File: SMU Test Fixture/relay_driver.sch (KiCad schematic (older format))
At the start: 48 parts, among them U7 ADG1414BRU, U8 ADG1414BRU

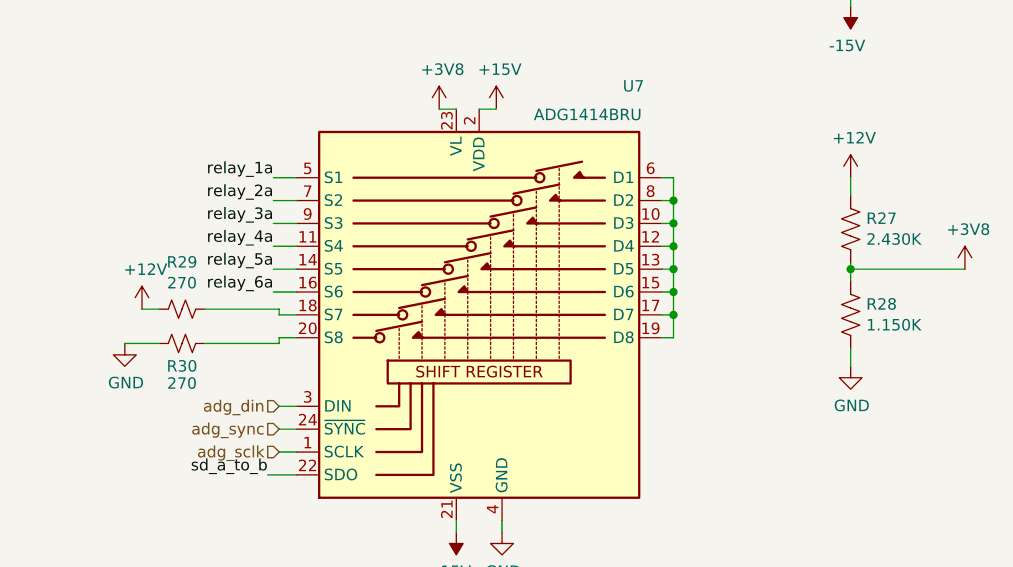
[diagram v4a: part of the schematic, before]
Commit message: Reannotate, power supply schematic improvements, begin power supply layout.
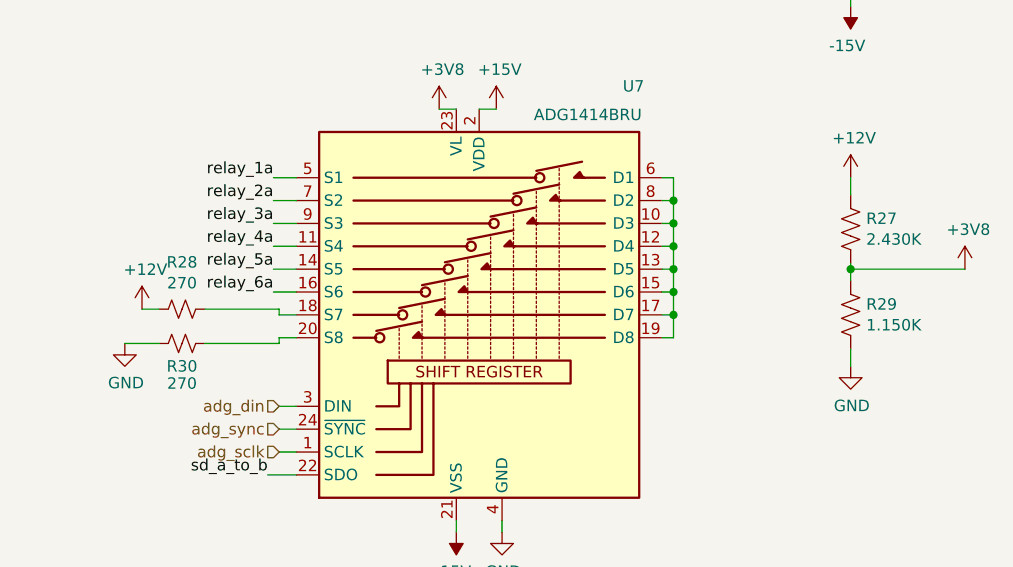
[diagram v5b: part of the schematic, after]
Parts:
- R27: footprint (none) -> Resistor_SMD:R_0805_2012Metric_Pad1.20x1.40mm_HandSolder
- R29: renamed from R28; footprint (none) -> Resistor_SMD:R_0805_2012Metric_Pad1.20x1.40mm_HandSolder
- renumbered R29 to R28
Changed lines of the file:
@@
 P 10425 700
 AR Path="/6011CEB7/6031CE6D" Ref="#PWR?"  Part="1"
-AR Path="/602F30C4/6031CE6D" Ref="#PWR046"  Part="1"
-F 0 "#PWR046" H 10425 550 50  0001 C CNN
+AR Path="/602F30C4/6031CE6D" Ref="#PWR045"  Part="1"
+F 0 "#PWR045" H 10425 550 50  0001 C CNN
 F 1 "+15V" H 10440 873 50  0000 C CNN
 F 2 "" H 10425 700 50  0001 C CNN
@@
 P 10425 1625
 AR Path="/6011CEB7/6031CE73" Ref="#PWR?"  Part="1"
-AR Path="/602F30C4/6031CE73" Ref="#PWR050"  Part="1"
-F 0 "#PWR050" H 10425 1725 50  0001 C CNN
+AR Path="/602F30C4/6031CE73" Ref="#PWR047"  Part="1"
+F 0 "#PWR047" H 10425 1725 50  0001 C CNN
 F 1 "-15V" H 10440 1798 50  0000 C CNN
 F 2 "" H 10425 1625 50  0001 C CNN
@@
 P 10200 1175
 AR Path="/6011CEB7/6031CE85" Ref="#PWR?"  Part="1"
-AR Path="/602F30C4/6031CE85" Ref="#PWR048"  Part="1"
-F 0 "#PWR048" H 10200 925 50  0001 C CNN
+AR Path="/602F30C4/6031CE85" Ref="#PWR046"  Part="1"
+F 0 "#PWR046" H 10200 925 50  0001 C CNN
 F 1 "GND" H 10205 1002 50  0000 C CNN
 F 2 "" H 10200 1175 50  0001 C CNN
@@
 	8000 2975 7925 2975
 $Comp
-L Device:R_Small_US R29
+L Device:R_Small_US R28
 U 1 1 63E80504
 P 7500 2950
-F 0 "R29" V 7295 2950 50  0000 C CNN
+F 0 "R28" V 7295 2950 50  0000 C CNN
 F 1 "270" V 7386 2950 50  0000 C CNN
 F 2 "Resistor_SMD:R_0805_2012Metric_Pad1.20x1.40mm_HandSolder" H 7500 2950 50  0001 C CNN
@@
 P 8875 2075
 AR Path="/6011CEB7/640AE01E" Ref="#PWR?"  Part="1"
-AR Path="/602F30C4/640AE01E" Ref="#PWR052"  Part="1"
-F 0 "#PWR052" H 8875 1925 50  0001 C CNN
+AR Path="/602F30C4/640AE01E" Ref="#PWR049"  Part="1"
+F 0 "#PWR049" H 8875 1925 50  0001 C CNN
 F 1 "+15V" H 8890 2248 50  0000 C CNN
 F 2 "" H 8875 2075 50  0001 C CNN
@@
 ext_meas_sel_b_r
 $Comp
-L power:GND #PWR054
+L power:GND #PWR053
 U 1 1 5FFD6724
 P 7250 3100
-F 0 "#PWR054" H 7250 2850 50  0001 C CNN
+F 0 "#PWR053" H 7250 2850 50  0001 C CNN
 F 1 "GND" H 7255 2927 50  0000 C CNN
 F 2 "" H 7250 3100 50  0001 C CNN
@@
 $EndComp
 $Comp
-L power:+12V #PWR053
+L power:+12V #PWR052
 U 1 1 60DAA752
 P 7325 2950
-F 0 "#PWR053" H 7325 2800 50  0001 C CNN
+F 0 "#PWR052" H 7325 2800 50  0001 C CNN
 F 1 "+12V" H 7340 3123 50  0000 C CNN
 F 2 "" H 7325 2950 50  0001 C CNN
@@
 F 0 "R27" H 10493 2646 50  0000 L CNN
 F 1 "2.430K" H 10493 2555 50  0000 L CNN
-F 2 "" V 10465 2590 50  0001 C CNN
+F 2 "Resistor_SMD:R_0805_2012Metric_Pad1.20x1.40mm_HandSolder" V 10465 2590 50  0001 C CNN
 F 3 "~" H 10425 2600 50  0001 C CNN
 	1    10425 2600
@@
 $EndComp
 $Comp
-L Device:R_US R28
+L Device:R_US R29
 U 1 1 60DD8B3F
 P 10425 2975
-F 0 "R28" H 10493 3021 50  0000 L CNN
+F 0 "R29" H 10493 3021 50  0000 L CNN
 F 1 "1.150K" H 10493 2930 50  0000 L CNN
-F 2 "" V 10465 2965 50  0001 C CNN
+F 2 "Resistor_SMD:R_0805_2012Metric_Pad1.20x1.40mm_HandSolder" V 10465 2965 50  0001 C CNN
 F 3 "~" H 10425 2975 50  0001 C CNN
 	1    10425 2975
@@
 $EndComp
 $Comp
-L power:GND #PWR049
+L power:GND #PWR054
 U 1 1 60DD9AAA
 P 10425 3200
-F 0 "#PWR049" H 10425 2950 50  0001 C CNN
+F 0 "#PWR054" H 10425 2950 50  0001 C CNN
 F 1 "GND" H 10430 3027 50  0000 C CNN
 F 2 "" H 10425 3200 50  0001 C CNN
@@
 $EndComp
 $Comp
-L power:+12V #PWR045
+L power:+12V #PWR050
 U 1 1 60DDA822
 P 10425 2375
-F 0 "#PWR045" H 10425 2225 50  0001 C CNN
+F 0 "#PWR050" H 10425 2225 50  0001 C CNN
 F 1 "+12V" H 10440 2548 50  0000 C CNN
 F 2 "" H 10425 2375 50  0001 C CNN
@@
 	10425 2450 10425 2375
 $Comp
-L power:+3V8 #PWR047
+L power:+3V8 #PWR051
 U 1 1 60E46539
 P 10925 2775
-F 0 "#PWR047" H 10925 2625 50  0001 C CNN
+F 0 "#PWR051" H 10925 2625 50  0001 C CNN
 F 1 "+3V8" H 10940 2948 50  0000 C CNN
 F 2 "" H 10925 2775 50  0001 C CNN
@@
 	10425 2775 10425 2750
 $Comp
-L power:+3V8 #PWR051
+L power:+3V8 #PWR048
 U 1 1 60E6B69C
 P 8625 2075
-F 0 "#PWR051" H 8625 1925 50  0001 C CNN
+F 0 "#PWR048" H 8625 1925 50  0001 C CNN
 F 1 "+3V8" H 8640 2248 50  0000 C CNN
 F 2 "" H 8625 2075 50  0001 C CNN

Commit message: Switch to TVS flyback diodes.
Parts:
- removed D10, D11, D12, D13, D14, D15, D16, D17, D18, D19, D2, D20, D21, D22, D23, D24, D25, D26, D27, D28, D29, D3, D30, D31, D32, D33, D34, D35, D36, D4, D5, D6, D7, D8, D9: Vz=+-15V, Package_TO_SOT_SMD:SOT-323_SC-70_Handsoldering, symbol Device:D_Zener_x2_ACom_AKK
- added D10, D11, D12, D13, D14, D15, D16, D17, D18, D19, D2, D20, D21, D22, D23, D24, D25, D26, D27, D28, D29, D3, D30, D31, D32, D33, D34, D35, D36, D4, D5, D6, D7, D8, D9: Vcl=14V, Diode_SMD:D_0201_0603Metric_Pad0.64x0.40mm_HandSolder, symbol Device:D_TVS
- D1: value Vz=+-15V -> Vcl=14V; footprint Package_TO_SOT_SMD:SOT-323_SC-70_Handsoldering -> Diode_SMD:D_0201_0603Metric_Pad0.64x0.40mm_HandSolder; symbol Device:D_Zener_x2_ACom_AKK -> Device:D_TVS; PN MMBZH15VAWT1G -> VS12VBA1HS
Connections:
- wire segments 380 -> 417
- no-connect marks 37 -> 1
